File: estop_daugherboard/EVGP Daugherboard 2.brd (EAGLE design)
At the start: 82.6 x 94.1 mm, 41 parts, among them J1 JST-XH-02-PIN-LONG-PAD, J2 JST-XH-02-PIN-LONG-PAD, J3 JST-XH-03-PIN-LONG-PAD, J4 JST-XH-03-PIN-LONG-PAD, J5 AVR_SPI_PROG_3X2PTH, J6 UX60-MB-5S8, J7 4_XH_JST, Q1 N_FET2, Q2 N_FET1, U1 NL27WZ08USG, U2 ATMEGA32U4-AU, X1 TSX-3225 16.0000MF18X-AC0

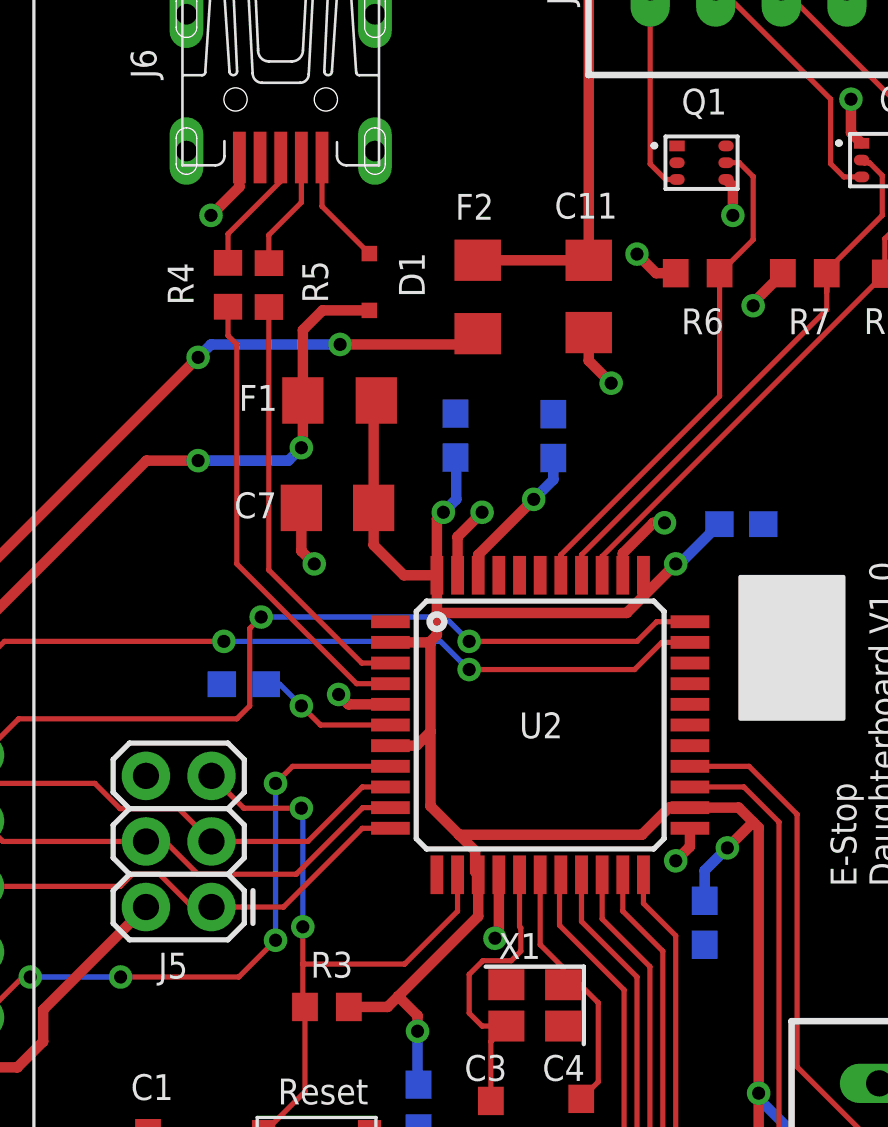
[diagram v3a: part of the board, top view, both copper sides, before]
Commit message: usb resistors moved out of conflict
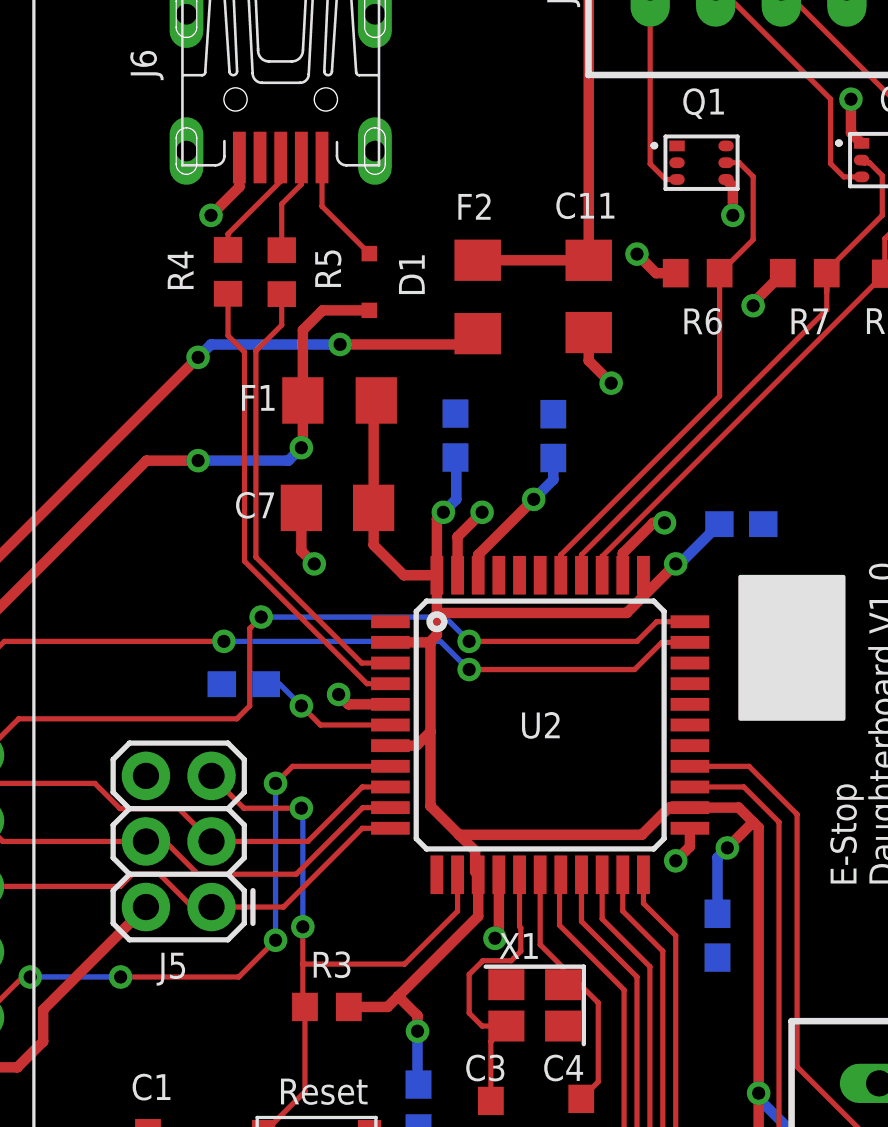
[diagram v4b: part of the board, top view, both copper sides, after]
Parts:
- moved C5 0.71 mm to (78.1, 48.1)
- moved R5 0.71 mm to (61.2, 73.8)
- moved R4 0.50 mm to (59.2, 73.8)
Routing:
- net DATA_N: track 16.4 -> 17.5 mm
- net N$5: track 4.61 -> 3.90 mm
- net N$11: track 4.92 -> 4.42 mm
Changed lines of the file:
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@@
 <drawing>
 <settings>
-<setting alwaysvectorfont="no"/>
+<setting alwaysvectorfont="yes"/>
 <setting verticaltext="up"/>
 </settings>
@@
 <attribute name="NAME" x="57.905" y="57.475" size="1" layer="26" font="vector" rot="MR0"/>
 </element>
-<element name="C5" library="resistor" library_urn="urn:adsk.eagle:library:348" package="C0603" package3d_urn="urn:adsk.eagle:package:23616/2" value="0.1 uF" x="77.62" y="48.6" smashed="yes" rot="MR270">
-<attribute name="NAME" x="78.465" y="45.585" size="1" layer="26" font="vector" rot="MR0"/>
+<element name="C5" library="resistor" library_urn="urn:adsk.eagle:library:348" package="C0603" package3d_urn="urn:adsk.eagle:package:23616/2" value="0.1 uF" x="78.12" y="48.1" smashed="yes" rot="MR270">
+<attribute name="NAME" x="78.965" y="45.085" size="1" layer="26" font="vector" rot="MR0"/>
 </element>
 <element name="C9" library="resistor" library_urn="urn:adsk.eagle:library:348" package="C0603" package3d_urn="urn:adsk.eagle:package:23616/2" value="10 nF" x="71.76" y="67.45" smashed="yes" rot="MR90">
@@
 <attribute name="SPICEPREFIX" value="R" x="99.82" y="-79.12" size="1.778" layer="27" display="off"/>
 </element>
-<element name="R5" library="rcl" library_urn="urn:adsk.eagle:library:334" package="R0603" package3d_urn="urn:adsk.eagle:package:23555/3" value="22 Ω" x="60.74" y="73.3" smashed="yes" rot="R90">
-<attribute name="NAME" x="63.035" y="72.605" size="1" layer="25" font="vector" rot="R90"/>
-<attribute name="POPULARITY" value="77" x="180.12" y="169.82" size="1.778" layer="27" rot="R90" display="off"/>
-<attribute name="SPICEPREFIX" value="R" x="180.12" y="169.82" size="1.778" layer="27" rot="R90" display="off"/>
-</element>
-<element name="R4" library="rcl" library_urn="urn:adsk.eagle:library:334" package="R0603" package3d_urn="urn:adsk.eagle:package:23555/3" value="22 Ω" x="59.16" y="73.31" smashed="yes" rot="R90">
-<attribute name="NAME" x="57.825" y="72.525" size="1" layer="25" font="vector" rot="R90"/>
-<attribute name="POPULARITY" value="77" x="183.62" y="89.82" size="1.778" layer="27" rot="R90" display="off"/>
-<attribute name="SPICEPREFIX" value="R" x="183.62" y="89.82" size="1.778" layer="27" rot="R90" display="off"/>
+<element name="R5" library="rcl" library_urn="urn:adsk.eagle:library:334" package="R0603" package3d_urn="urn:adsk.eagle:package:23555/3" value="22 Ω" x="61.24" y="73.8" smashed="yes" rot="R90">
+<attribute name="NAME" x="63.535" y="73.105" size="1" layer="25" font="vector" rot="R90"/>
+<attribute name="POPULARITY" value="77" x="180.62" y="170.32" size="1.778" layer="27" rot="R90" display="off"/>
+<attribute name="SPICEPREFIX" value="R" x="180.62" y="170.32" size="1.778" layer="27" rot="R90" display="off"/>
+</element>
+<element name="R4" library="rcl" library_urn="urn:adsk.eagle:library:334" package="R0603" package3d_urn="urn:adsk.eagle:package:23555/3" value="22 Ω" x="59.16" y="73.81" smashed="yes" rot="R90">
+<attribute name="NAME" x="57.825" y="73.025" size="1" layer="25" font="vector" rot="R90"/>
+<attribute name="POPULARITY" value="77" x="183.62" y="90.32" size="1.778" layer="27" rot="R90" display="off"/>
+<attribute name="SPICEPREFIX" value="R" x="183.62" y="90.32" size="1.778" layer="27" rot="R90" display="off"/>
 </element>
 <element name="R1" library="rcl" library_urn="urn:adsk.eagle:library:334" package="R0603" package3d_urn="urn:adsk.eagle:package:23555/3" value="330Ω" x="74.74" y="19.4" smashed="yes" rot="R90">
@@
 <wire x1="78.5" y1="51.5" x2="79.5" y2="52.5" width="0.4064" layer="1"/>
 <via x="78.5" y="51.5" extent="1-16" drill="0.508"/>
-<wire x1="78.5" y1="51.5" x2="77.62" y2="50.62" width="0.4064" layer="16"/>
-<wire x1="77.62" y1="50.62" x2="77.62" y2="49.45" width="0.4064" layer="16"/>
+<wire x1="78.5" y1="51.5" x2="78.12" y2="51.12" width="0.4064" layer="16"/>
+<wire x1="78.12" y1="51.12" x2="78.12" y2="48.95" width="0.4064" layer="16"/>
 <via x="76.5" y="62.5" extent="1-16" drill="0.508"/>
 <wire x1="76.5" y1="62.5" x2="76.65" y2="62.5" width="0.4064" layer="16"/>
@@
 <contactref element="R5" pad="1"/>
 <contactref element="U2" pad="3"/>
-<wire x1="60.74" y1="72.45" x2="60.74" y2="62.26" width="0.2032" layer="1"/>
+<wire x1="61.24" y1="72.95" x2="61.24" y2="71.75" width="0.2032" layer="1"/>
+<wire x1="61.24" y1="71.75" x2="60.24" y2="70.75" width="0.2032" layer="1"/>
+<wire x1="60.24" y1="70.75" x2="60.24" y2="62.76" width="0.2032" layer="1"/>
 <wire x1="64.34" y1="58.66" x2="65.45" y2="58.66" width="0.2032" layer="1"/>
-<wire x1="60.74" y1="62.26" x2="64.34" y2="58.66" width="0.2032" layer="1"/>
+<wire x1="60.24" y1="62.76" x2="64.34" y2="58.66" width="0.2032" layer="1"/>
 </signal>
 <signal name="DATA_P" class="2">
 <contactref element="R4" pad="1"/>
 <contactref element="U2" pad="4"/>
-<wire x1="64.14" y1="57.86" x2="65.45" y2="57.86" width="0.2032" layer="1"/>
-<wire x1="59.5" y1="71" x2="59.5" y2="62.5" width="0.2032" layer="1"/>
-<wire x1="59.5" y1="62.5" x2="64.14" y2="57.86" width="0.2032" layer="1"/>
-<wire x1="59.16" y1="72.46" x2="59.16" y2="71.34" width="0.2032" layer="1"/>
-<wire x1="59.16" y1="71.34" x2="59.5" y2="71" width="0.2032" layer="1"/>
+<wire x1="64.54" y1="57.86" x2="65.45" y2="57.86" width="0.2032" layer="1"/>
+<wire x1="59.8" y1="70.7" x2="59.8" y2="62.6" width="0.2032" layer="1"/>
+<wire x1="59.8" y1="62.6" x2="64.54" y2="57.86" width="0.2032" layer="1"/>
+<wire x1="59.16" y1="72.96" x2="59.16" y2="71.34" width="0.2032" layer="1"/>
+<wire x1="59.16" y1="71.34" x2="59.8" y2="70.7" width="0.2032" layer="1"/>
 </signal>
 <signal name="N$7">
@@
 <contactref element="J6" pad="2"/>
 <contactref element="R5" pad="2"/>
-<wire x1="62" y1="76.5" x2="62" y2="78.24" width="0.2032" layer="1"/>
-<wire x1="60.74" y1="74.15" x2="60.74" y2="75.24" width="0.2032" layer="1"/>
-<wire x1="60.74" y1="75.24" x2="62" y2="76.5" width="0.2032" layer="1"/>
+<wire x1="62" y1="77.2" x2="62" y2="78.24" width="0.2032" layer="1"/>
+<wire x1="61.24" y1="74.65" x2="61.24" y2="76.44" width="0.2032" layer="1"/>
+<wire x1="61.24" y1="76.44" x2="62" y2="77.2" width="0.2032" layer="1"/>
 </signal>
 <signal name="N$11">
 <contactref element="J6" pad="3"/>
 <contactref element="R4" pad="2"/>
-<wire x1="59.16" y1="74.16" x2="59.16" y2="75.283025" width="0.2032" layer="1"/>
+<wire x1="59.16" y1="74.66" x2="59.16" y2="75.283025" width="0.2032" layer="1"/>
 <wire x1="61.2" y1="77.323025" x2="61.2" y2="78.24" width="0.2032" layer="1"/>
 <wire x1="59.16" y1="75.283025" x2="61.2" y2="77.323025" width="0.2032" layer="1"/>

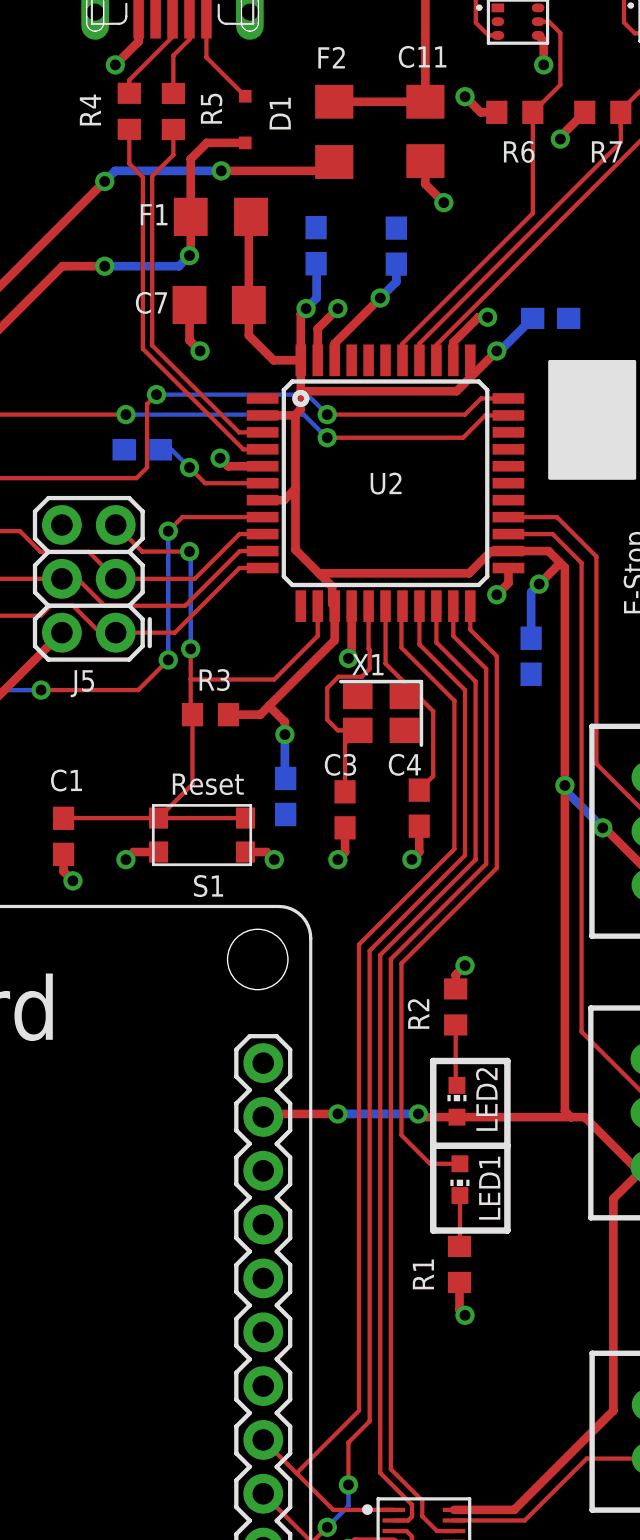
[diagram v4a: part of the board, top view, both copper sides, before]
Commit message: Changed led2 name
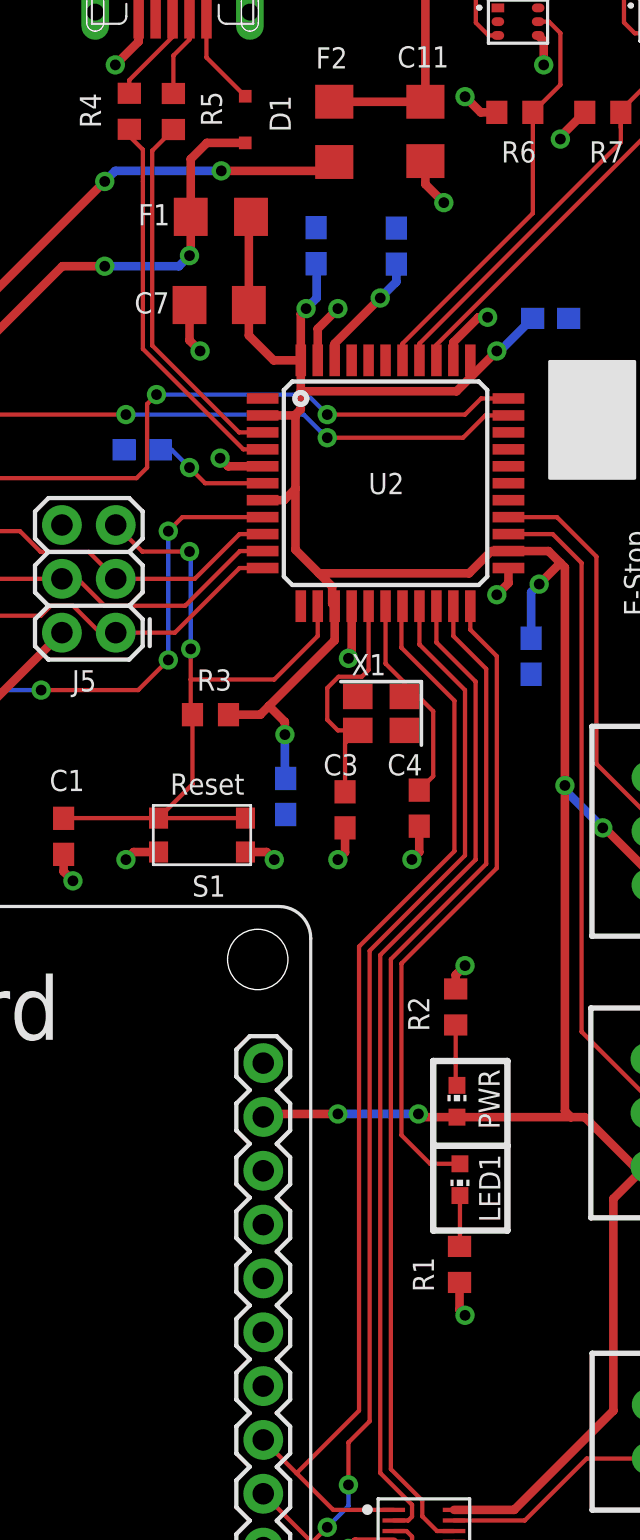
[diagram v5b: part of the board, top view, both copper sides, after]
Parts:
- renumbered LED2 to PWR
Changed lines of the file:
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@@
 <?xml version="1.0" encoding="utf-8"?>
 <!DOCTYPE eagle SYSTEM "eagle.dtd">
-<eagle version="9.5.0">
+<eagle version="9.5.1">
 <drawing>
 <settings>
-<setting alwaysvectorfont="yes"/>
+<setting alwaysvectorfont="no"/>
 <setting verticaltext="up"/>
 </settings>
@@
 <attribute name="NAME" x="72.525" y="84.13" size="1" layer="25" font="vector" rot="R90"/>
 </element>
-<element name="LED2" library="led" library_urn="urn:adsk.eagle:library:259" package="CHIP-LED0603" package3d_urn="urn:adsk.eagle:package:15819/3" value="GREEN" x="74.62" y="27.1" smashed="yes">
-<attribute name="NAME" x="76.535" y="25.585" size="1" layer="25" font="vector" rot="R90"/>
+<element name="PWR" library="led" library_urn="urn:adsk.eagle:library:259" package="CHIP-LED0603" package3d_urn="urn:adsk.eagle:package:15819/3" value="GREEN" x="74.62" y="27.1" smashed="yes">
+<attribute name="NAME" x="76.635" y="25.785" size="1" layer="25" font="vector" rot="R90"/>
 <attribute name="POPULARITY" value="26" x="74.62" y="27.1" size="1.778" layer="27" display="off"/>
 </element>
@@
 </signal>
 <signal name="5V" class="1">
-<contactref element="LED2" pad="A"/>
+<contactref element="PWR" pad="A"/>
 <contactref element="U2" pad="14"/>
 <contactref element="U2" pad="34"/>
@@
 <signal name="N$3">
 <contactref element="R2" pad="2"/>
-<contactref element="LED2" pad="C"/>
+<contactref element="PWR" pad="C"/>
 <wire x1="74.62" y1="27.85" x2="74.56" y2="27.91" width="0.2032" layer="1"/>
 <wire x1="74.56" y1="27.91" x2="74.56" y2="30.7" width="0.2032" layer="1"/>
@@
 <wire x1="69.34" y1="44" x2="69.94" y2="44.6" width="0.2032" layer="1"/>
 <wire x1="69.94" y1="44.6" x2="69" y2="44.6" width="0.2032" layer="1"/>
-<wire x1="70.45" y1="50.46" x2="70.45" y2="48.45" width="0.2032" layer="1"/>
-<wire x1="70.45" y1="48.45" x2="70.5" y2="48.4" width="0.2032" layer="1"/>
-<wire x1="70.5" y1="48.4" x2="70.5" y2="47.5" width="0.2032" layer="1"/>
-<wire x1="70.5" y1="47.5" x2="70.1302" y2="47.1302" width="0.2032" layer="1"/>
+<wire x1="70.45" y1="50.46" x2="70.45" y2="47.45" width="0.2032" layer="1"/>
+<wire x1="70.45" y1="47.45" x2="70.1302" y2="47.1302" width="0.2032" layer="1"/>
 <wire x1="69.0302" y1="47.1302" x2="70.1302" y2="47.1302" width="0.2032" layer="1"/>
 <wire x1="69" y1="44.6" x2="68.5" y2="45.1" width="0.2032" layer="1"/>
@@
 <contactref element="R5" pad="1"/>
 <contactref element="U2" pad="3"/>
-<wire x1="61.24" y1="72.95" x2="61.24" y2="71.75" width="0.2032" layer="1"/>
-<wire x1="61.24" y1="71.75" x2="60.24" y2="70.75" width="0.2032" layer="1"/>
-<wire x1="60.24" y1="70.75" x2="60.24" y2="62.76" width="0.2032" layer="1"/>
 <wire x1="64.34" y1="58.66" x2="65.45" y2="58.66" width="0.2032" layer="1"/>
-<wire x1="60.24" y1="62.76" x2="64.34" y2="58.66" width="0.2032" layer="1"/>
+<wire x1="64.34" y1="58.66" x2="60.24" y2="62.76" width="0.2032" layer="1"/>
+<wire x1="60.24" y1="71.95" x2="61.24" y2="72.95" width="0.2032" layer="1"/>
+<wire x1="60.24" y1="62.76" x2="60.24" y2="71.95" width="0.2032" layer="1"/>
 </signal>
 <signal name="DATA_P" class="2">
@@
 <contactref element="U2" pad="4"/>
 <wire x1="64.54" y1="57.86" x2="65.45" y2="57.86" width="0.2032" layer="1"/>
-<wire x1="59.8" y1="70.7" x2="59.8" y2="62.6" width="0.2032" layer="1"/>
+<wire x1="59.8" y1="70.7" x2="59.8" y2="70.5" width="0.2032" layer="1"/>
+<wire x1="59.8" y1="70.5" x2="59.8" y2="62.6" width="0.2032" layer="1"/>
 <wire x1="59.8" y1="62.6" x2="64.54" y2="57.86" width="0.2032" layer="1"/>
-<wire x1="59.16" y1="72.96" x2="59.16" y2="71.34" width="0.2032" layer="1"/>
-<wire x1="59.16" y1="71.34" x2="59.8" y2="70.7" width="0.2032" layer="1"/>
+<wire x1="59.8" y1="70.7" x2="59.8" y2="72" width="0.2032" layer="1"/>
+<wire x1="59.16" y1="72.64" x2="59.16" y2="72.96" width="0.2032" layer="1"/>
+<wire x1="59.8" y1="72" x2="59.16" y2="72.64" width="0.2032" layer="1"/>
 </signal>
 <signal name="N$7">
@@
 <wire x1="67.05" y1="9.55" x2="65.48" y2="11.12" width="0.2032" layer="1"/>
 <wire x1="67.05" y1="9.55" x2="70" y2="12.5" width="0.2032" layer="1"/>
-<wire x1="70" y1="34.5" x2="74.5" y2="39" width="0.2032" layer="1"/>
-<wire x1="74.5" y1="39" x2="74.5" y2="46" width="0.2032" layer="1"/>
+<wire x1="70" y1="34.4" x2="74.5" y2="38.9" width="0.2032" layer="1"/>
+<wire x1="74.5" y1="38.9" x2="74.5" y2="46" width="0.2032" layer="1"/>
 <wire x1="74.5" y1="46" x2="72" y2="48.5" width="0.2032" layer="1"/>
 <wire x1="72" y1="48.5" x2="72" y2="50.41" width="0.2032" layer="1"/>
 <wire x1="72" y1="50.41" x2="72.05" y2="50.46" width="0.2032" layer="1"/>
-<wire x1="70" y1="12.5" x2="70" y2="34.5" width="0.2032" layer="1"/>
+<wire x1="70" y1="12.5" x2="70" y2="34.4" width="0.2032" layer="1"/>
 </signal>
 <signal name="DRIVE_EN_DB">
